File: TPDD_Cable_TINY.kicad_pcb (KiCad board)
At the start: 2 copper layers, 8.9 x 7.7 mm, 5 parts, among them J1 Conn_01x07, J2 TPDD, Q1 DTA114E, Q2 DTA114E, Q3 DTA114E

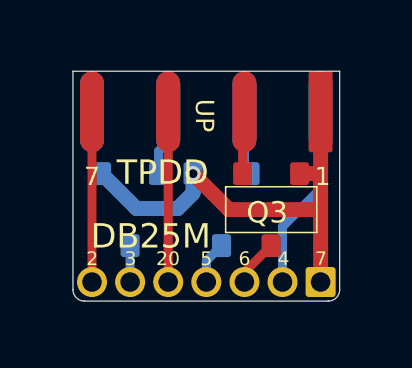
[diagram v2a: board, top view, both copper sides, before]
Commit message: bigger 2x4 solder pads, smaller wire holes
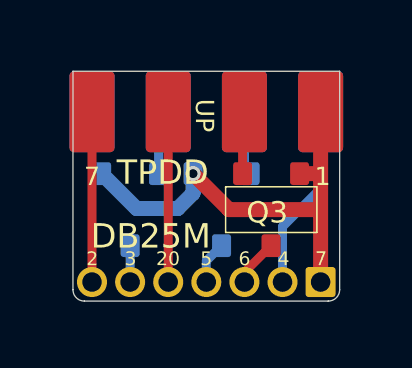
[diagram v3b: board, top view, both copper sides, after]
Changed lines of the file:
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@@
-(kicad_pcb (version 20171130) (host pcbnew 5.1.9-73d0e3b20d~88~ubuntu20.10.1)
+(kicad_pcb (version 20171130) (host pcbnew 5.1.10-88a1d61d58~88~ubuntu20.10.1)
   (general
     (thickness 1.6)
@@
     (add_net GNDS)
   )
+  (module 000_LOCAL:2-6-2_tpdd (layer Top)
+    (at 148.803 82.9065)
+    (attr smd)
+    (fp_text reference J2 (at -1.27 -0.127 -90 unlocked) (layer F.SilkS) hide
+      (effects (font (size 0.6096 0.6096) (thickness 0.0508)))
+    )
+    (fp_text value TPDD (at -3.81 2.286) (layer F.Fab)
+      (effects (font (size 0.4572 0.4572) (thickness 0.00254)))
+    )
+    (fp_text user 8 (at -7.874 2.159 unlocked) (layer B.SilkS)
+      (effects (font (size 0.6096 0.6096) (thickness 0.0762)) (justify mirror))
+    )
+    (fp_text user 2 (at 0 2.159 unlocked) (layer B.SilkS)
+      (effects (font (size 0.6096 0.6096) (thickness 0.0762)) (justify mirror))
+    )
+    (fp_text user 7 (at -7.62 2.159 unlocked) (layer F.SilkS)
+      (effects (font (size 0.6096 0.6096) (thickness 0.0762)))
+    )
+    (fp_text user 1 (at 0.0635 2.159 unlocked) (layer F.SilkS)
+      (effects (font (size 0.6096 0.6096) (thickness 0.0762)))
+    )
+    (pad 2 smd roundrect (at 0 0) (size 1.5 2.7) (layers Bottom B.Mask) (roundrect_rratio 0.1)
+      (net 2 /RTS))
+    (pad 4 smd roundrect (at -2.54 0) (size 1.5 2.7) (layers Bottom B.Mask) (roundrect_rratio 0.1)
+      (net 8 /CTS_TTL))
+    (pad 6 smd roundrect (at -5.08 0) (size 1.5 2.7) (layers Bottom B.Mask) (roundrect_rratio 0.1)
+      (net 7 /RX_TTL))
+    (pad 8 smd roundrect (at -7.62 0) (size 1.5 2.7) (layers Bottom B.Mask) (roundrect_rratio 0.1))
+    (pad 7 smd roundrect (at -7.62 0) (size 1.5 2.7) (layers Top F.Mask) (roundrect_rratio 0.1)
+      (net 10 /TX))
+    (pad 5 smd roundrect (at -5.08 0) (size 1.5 2.7) (layers Top F.Mask) (roundrect_rratio 0.1)
+      (net 6 /DTR))
+    (pad 3 smd roundrect (at -2.54 0) (size 1.5 2.7) (layers Top F.Mask) (roundrect_rratio 0.1)
+      (net 9 /DSR_TTL))
+    (pad 1 smd roundrect (at 0 0) (size 1.5 2.7) (layers Top F.Mask) (roundrect_rratio 0.1)
+      (net 5 GNDS))
+    (model ${KIPRJMOD}/000_LOCAL.pretty/3dshapes/PinSocket_2x03_P2.54mm_Vertical_2pulled.step
+      (offset (xyz -5.08 1.47 2.93))
+      (scale (xyz 1 1 1))
+      (rotate (xyz 90 180 0))
+    )
+    (model ${KIPRJMOD}/000_LOCAL.pretty/3dshapes/PinSocket_1x02_P2.54mm_Vertical.step
+      (offset (xyz 0 1.47 -2.15))
+      (scale (xyz 1 1 1))
+      (rotate (xyz 90 0 0))
+    )
+    (model ${KIPRJMOD}/000_LOCAL.pretty/3dshapes/PinSocket_1x02_P2.54mm_Vertical.step
+      (offset (xyz -7.62 1.47 -2.15))
+      (scale (xyz 1 1 1))
+      (rotate (xyz 90 0 0))
+    )
+  )
   (module 000_LOCAL:1x7x2mm (layer Top)
     (at 146.263 86.8045)
@@
       (effects (font (size 1.2065 1.2065) (thickness 0.1016)) (justify right top mirror))
     )
+    (fp_line (start 0.762 1.524) (end 0.762 -1.516) (layer B.SilkS) (width 0.0508))
+    (fp_line (start -0.762 1.524) (end -0.762 -1.516) (layer B.SilkS) (width 0.0508))
+    (fp_line (start -0.762 1.524) (end 0.762 1.524) (layer B.SilkS) (width 0.0508))
+    (fp_line (start -0.762 -1.516) (end 0.762 -1.516) (layer B.SilkS) (width 0.0508))
     (fp_text user %R (at 0 0) (layer B.Fab) hide
       (effects (font (size 0.5 0.5) (thickness 0.075)) (justify mirror))
     )
-    (fp_line (start -0.762 -1.516) (end 0.762 -1.516) (layer B.SilkS) (width 0.0508))
-    (fp_line (start -0.762 1.524) (end 0.762 1.524) (layer B.SilkS) (width 0.0508))
-    (fp_line (start -0.762 1.524) (end -0.762 -1.516) (layer B.SilkS) (width 0.0508))
-    (fp_line (start 0.762 1.524) (end 0.762 -1.516) (layer B.SilkS) (width 0.0508))
     (pad 1 smd roundrect (at -1.2 0.95 270) (size 0.762 0.635) (layers Bottom B.Paste B.Mask) (roundrect_rratio 0.15)
       (net 5 GNDS))
@@
       (effects (font (size 1.2065 1.2065) (thickness 0.1016)) (justify right top mirror))
     )
+    (fp_line (start 0.762 1.524) (end 0.762 -1.516) (layer B.SilkS) (width 0.0508))
+    (fp_line (start -0.762 1.524) (end -0.762 -1.516) (layer B.SilkS) (width 0.0508))
+    (fp_line (start -0.762 1.524) (end 0.762 1.524) (layer B.SilkS) (width 0.0508))
+    (fp_line (start -0.762 -1.516) (end 0.762 -1.516) (layer B.SilkS) (width 0.0508))
     (fp_text user %R (at 0 0) (layer B.Fab) hide
       (effects (font (size 0.5 0.5) (thickness 0.075)) (justify mirror))
     )
-    (fp_line (start -0.762 -1.516) (end 0.762 -1.516) (layer B.SilkS) (width 0.0508))
-    (fp_line (start -0.762 1.524) (end 0.762 1.524) (layer B.SilkS) (width 0.0508))
-    (fp_line (start -0.762 1.524) (end -0.762 -1.516) (layer B.SilkS) (width 0.0508))
-    (fp_line (start 0.762 1.524) (end 0.762 -1.516) (layer B.SilkS) (width 0.0508))
     (pad 1 smd roundrect (at -1.2 0.95 270) (size 0.762 0.635) (layers Bottom B.Paste B.Mask) (roundrect_rratio 0.15)
       (net 5 GNDS))
@@
       (effects (font (size 1.2065 1.2065) (thickness 0.1016)) (justify right top))
     )
+    (fp_line (start 0.762 -1.524) (end 0.762 1.516) (layer F.SilkS) (width 0.0508))
+    (fp_line (start -0.762 -1.524) (end -0.762 1.516) (layer F.SilkS) (width 0.0508))
+    (fp_line (start -0.762 -1.524) (end 0.762 -1.524) (layer F.SilkS) (width 0.0508))
+    (fp_line (start -0.762 1.516) (end 0.762 1.516) (layer F.SilkS) (width 0.0508))
     (fp_text user %R (at 0 0) (layer F.Fab) hide
       (effects (font (size 0.5 0.5) (thickness 0.075)))
     )
-    (fp_line (start -0.762 1.516) (end 0.762 1.516) (layer F.SilkS) (width 0.0508))
-    (fp_line (start -0.762 -1.524) (end 0.762 -1.524) (layer F.SilkS) (width 0.0508))
-    (fp_line (start -0.762 -1.524) (end -0.762 1.516) (layer F.SilkS) (width 0.0508))
-    (fp_line (start 0.762 -1.524) (end 0.762 1.516) (layer F.SilkS) (width 0.0508))
     (pad 1 smd roundrect (at -1.2 -0.95 270) (size 0.762 0.635) (layers Top F.Paste F.Mask) (roundrect_rratio 0.15)
       (net 5 GNDS))
@@
     )
   )
-  (module 000_LOCAL:2-6-2_tpdd (layer Top)
-    (at 148.803 82.9065)
-    (attr smd)
-    (fp_text reference J2 (at -1.27 -0.127 -90 unlocked) (layer F.SilkS) hide
-      (effects (font (size 0.6096 0.6096) (thickness 0.0508)))
-    )
-    (fp_text value TPDD (at -3.81 2.286) (layer F.Fab)
-      (effects (font (size 0.4572 0.4572) (thickness 0.00254)))
-    )
-    (fp_text user 8 (at -7.874 2.159 unlocked) (layer B.SilkS)
-      (effects (font (size 0.6096 0.6096) (thickness 0.0762)) (justify mirror))
-    )
-    (fp_text user 2 (at 0 2.159 unlocked) (layer B.SilkS)
-      (effects (font (size 0.6096 0.6096) (thickness 0.0762)) (justify mirror))
-    )
-    (fp_text user 7 (at -7.62 2.159 unlocked) (layer F.SilkS)
-      (effects (font (size 0.6096 0.6096) (thickness 0.0762)))
-    )
-    (fp_text user 1 (at 0.0635 2.159 unlocked) (layer F.SilkS)
-      (effects (font (size 0.6096 0.6096) (thickness 0.0762)))
-    )
-    (pad 2 smd oval (at 0 0) (size 0.8 2.7) (layers Bottom B.Mask)
-      (net 2 /RTS))
-    (pad 4 smd oval (at -2.54 0) (size 0.8 2.7) (layers Bottom B.Mask)
-      (net 8 /CTS_TTL))
-    (pad 6 smd oval (at -5.08 0) (size 0.8 2.7) (layers Bottom B.Mask)
-      (net 7 /RX_TTL))
-    (pad 8 smd oval (at -7.62 0) (size 0.8 2.7) (layers Bottom B.Mask))
-    (pad 7 smd oval (at -7.62 0) (size 0.8 2.7) (layers Top F.Paste F.Mask)
-      (net 10 /TX))
-    (pad 5 smd oval (at -5.08 0) (size 0.8 2.7) (layers Top F.Paste F.Mask)
-      (net 6 /DTR))
-    (pad 3 smd oval (at -2.54 0) (size 0.8 2.7) (layers Top F.Paste F.Mask)
-      (net 9 /DSR_TTL))
-    (pad 1 smd roundrect (at 0 0) (size 0.8 2.7) (layers Top F.Paste F.Mask) (roundrect_rratio 0.1)
-      (net 5 GNDS))
-    (model ${KIPRJMOD}/000_LOCAL.pretty/3dshapes/PinSocket_2x03_P2.54mm_Vertical_2pulled.step
-      (offset (xyz -5.08 1.47 2.93))
-      (scale (xyz 1 1 1))
-      (rotate (xyz 90 180 0))
-    )
-    (model ${KIPRJMOD}/000_LOCAL.pretty/3dshapes/PinSocket_1x02_P2.54mm_Vertical.step
-      (offset (xyz 0 1.47 -2.15))
-      (scale (xyz 1 1 1))
-      (rotate (xyz 90 0 0))
-    )
-    (model ${KIPRJMOD}/000_LOCAL.pretty/3dshapes/PinSocket_1x02_P2.54mm_Vertical.step
-      (offset (xyz -7.62 1.47 -2.15))
-      (scale (xyz 1 1 1))
-      (rotate (xyz 90 0 0))
-    )
-  )

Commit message: kicad 6, ground zones
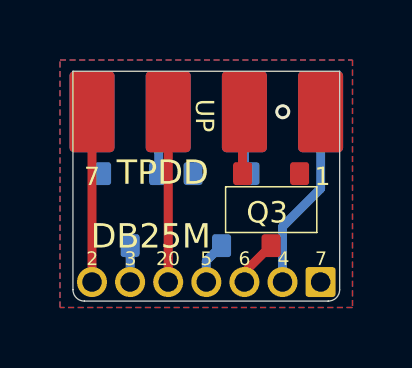
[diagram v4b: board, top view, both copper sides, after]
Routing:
- net GNDS: track 15.5 -> 0.00 mm
- added copper zone on B.Cu, net GNDS
- added copper zone on F.Cu, net GNDS
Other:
- net class Default removed
